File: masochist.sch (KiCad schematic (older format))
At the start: 76 parts, among them J1 USB_C_Receptacle_USB2.0, J2 AVR-ISP-6, SW1 RESET, SW2 SW_Push, U1 ATmega328P-PU, Y1 Crystal

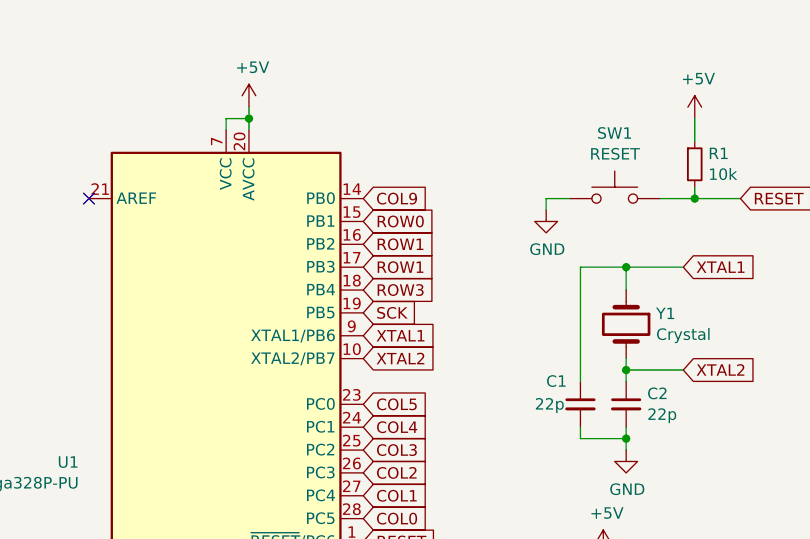
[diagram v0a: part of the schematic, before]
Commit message: updated pin assignments to make routing easier
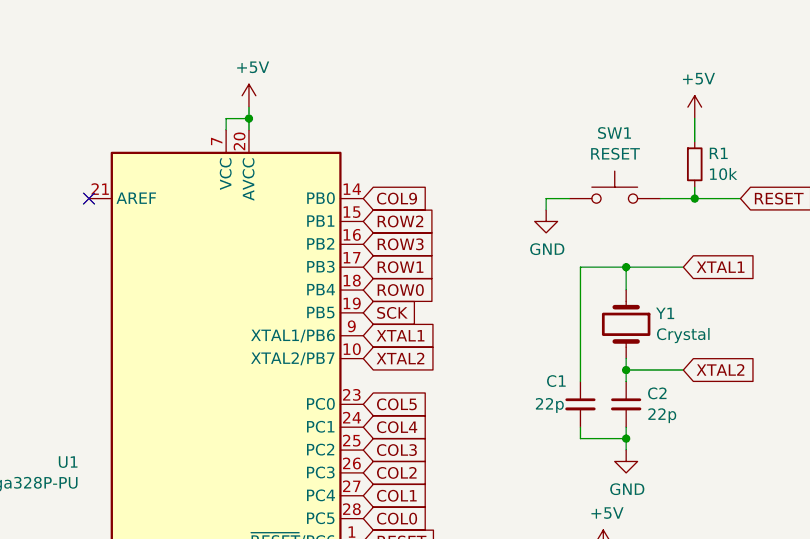
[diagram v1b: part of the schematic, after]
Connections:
- net ROW0: now also U1.18 (PB4); no longer U1.15 (PB1)
- net ROW1: no longer U1.16 (PB2)
- net ROW2: now also U1.15 (PB1)
- net ROW3: now also U1.16 (PB2); no longer U1.18 (PB4)
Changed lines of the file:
@@
 Wire Wire Line
 	1600 850  1600 900
-Text GLabel 2100 1300 2    50   Input ~ 0
+Text GLabel 2100 1600 2    50   Input ~ 0
 ROW0
-Text GLabel 2100 1400 2    50   Input ~ 0
-ROW1
 Text GLabel 2100 1500 2    50   Input ~ 0
 ROW1
-Text GLabel 2100 1600 2    50   Input ~ 0
+Text GLabel 2100 1400 2    50   Input ~ 0
 ROW3
 Text GLabel 2100 2600 2    50   Input ~ 0
@@
 Text GLabel 2100 3400 2    50   Input ~ 0
 BOOT
+Text GLabel 2100 1300 2    50   Input ~ 0
+ROW2
 $EndSCHEMATC

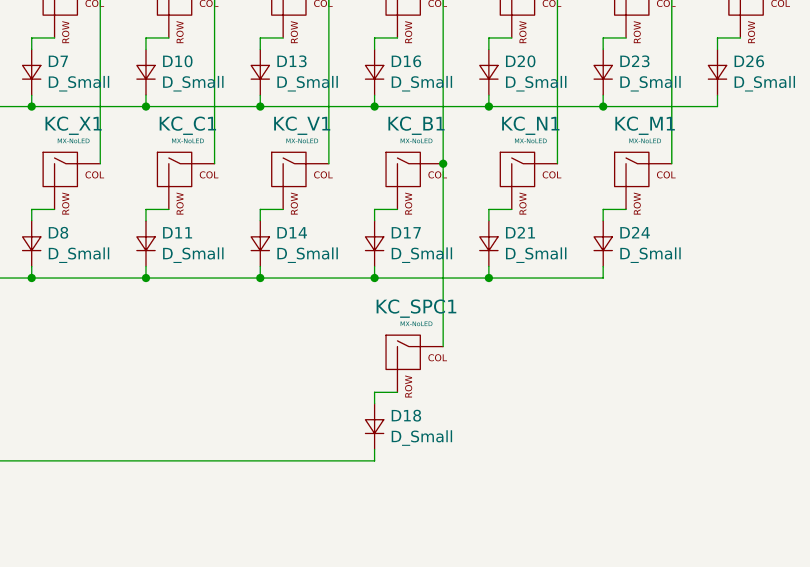
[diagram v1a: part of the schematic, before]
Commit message: Flipped spacebar and rerouted traces
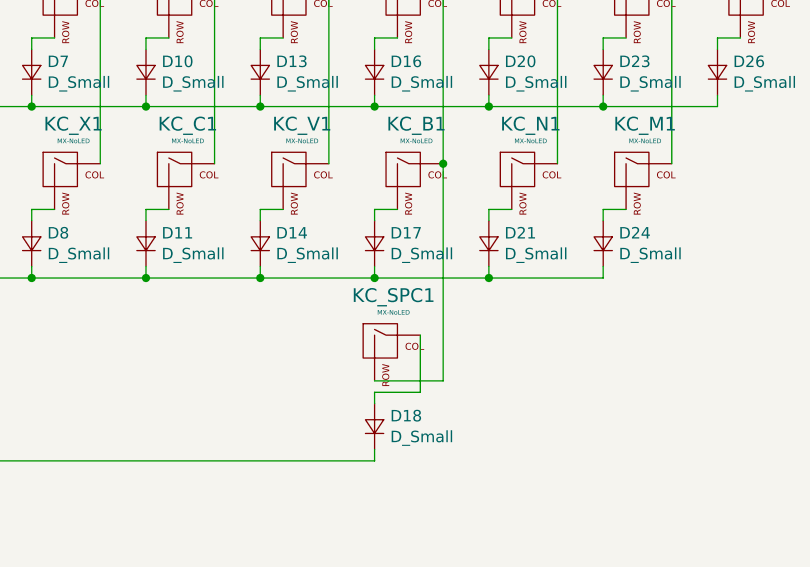
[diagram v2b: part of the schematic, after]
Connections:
- net COL5: now also KC_SPC1.2 (ROW); no longer KC_SPC1.1 (COL)
- net at D18.2 (A): now also KC_SPC1.1 (COL); no longer KC_SPC1.2 (ROW)
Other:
- moved on the sheet: KC_SPC1
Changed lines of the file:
@@
 L MX_Alps_Hybrid:MX-NoLED KC_SPC1
 U 1 1 5ECAC523
-P 8950 3550
-F 0 "KC_SPC1" H 8983 3773 60  0000 C CNN
-F 1 "MX-NoLED" H 8983 3699 20  0000 C CNN
-F 2 "MX_Only:MXOnly-6.25U-NoLED" H 8325 3525 60  0001 C CNN
-F 3 "" H 8325 3525 60  0001 C CNN
-	1    8950 3550
+P 8850 3500
+F 0 "KC_SPC1" H 8883 3723 60  0000 C CNN
+F 1 "MX-NoLED" H 8883 3649 20  0000 C CNN
+F 2 "MX_Only:MXOnly-6.25U-NoLED" H 8225 3475 60  0001 C CNN
+F 3 "" H 8225 3475 60  0001 C CNN
+	1    8850 3500
 	1    0    0    -1
 $EndComp
@@
 	8800 3750 8800 3700
 Wire Wire Line
-	8800 3700 8900 3700
-Wire Wire Line
 	10300 1600 10300 1650
 Connection ~ 10300 1650
@@
 	9100 2700 9100 1950
 Connection ~ 9100 1950
-Wire Wire Line
-	9100 3500 9100 2700
 Connection ~ 9100 2700
 Text GLabel 5850 4000 0    50   Input ~ 0
@@
 Text GLabel 2100 1300 2    50   Input ~ 0
 ROW2
+Wire Wire Line
+	9000 3700 9000 3450
+Wire Wire Line
+	8800 3700 9000 3700
+Wire Wire Line
+	9100 3650 8800 3650
+Wire Wire Line
+	9100 2700 9100 3650
 $EndSCHEMATC
